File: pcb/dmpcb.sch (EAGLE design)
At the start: 63 parts, among them IC1 7805DT, IC2 L293D, IC3 MAX7219CNG, IC4 LM358D, IC5 LM358D, J7 SJ-3523-SMT-TR, Q1 IRF530, Q2 IRF530

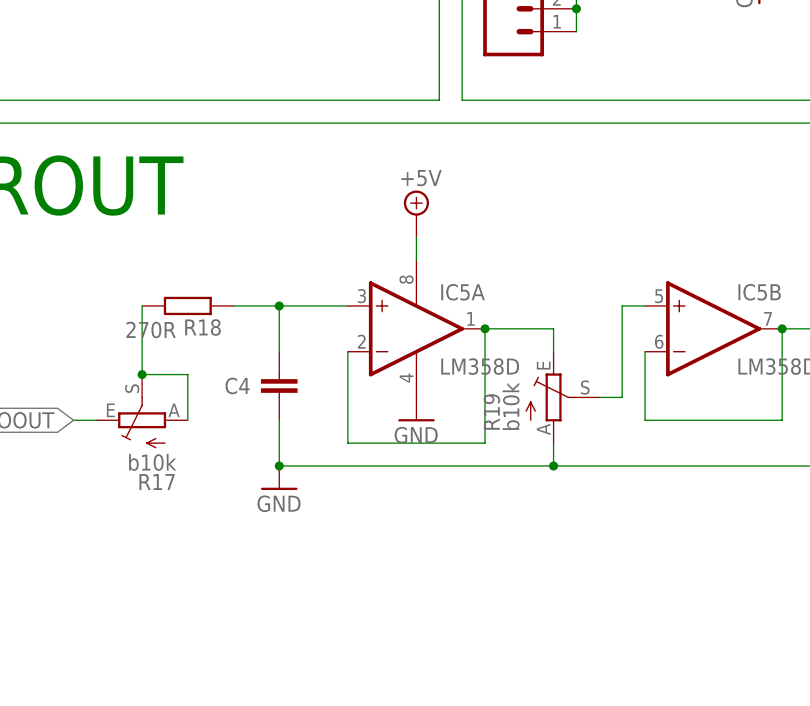
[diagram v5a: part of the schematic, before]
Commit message: added missing decoupling cap
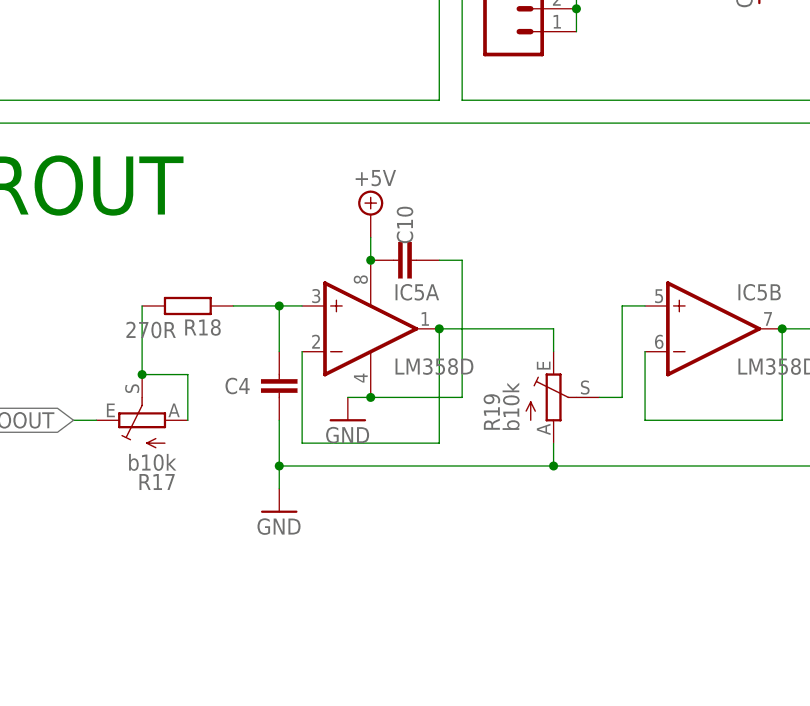
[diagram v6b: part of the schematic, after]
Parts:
- added C10: 100nf, rcl:C-EUC0805
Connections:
- net +5V: now also C10.2
- net GND: now also C10.1
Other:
- moved on the sheet: IC5A
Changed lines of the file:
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@@
 <part name="GND26" library="supply1" library_urn="urn:adsk.eagle:library:371" deviceset="GND" device=""/>
 <part name="GND28" library="supply1" library_urn="urn:adsk.eagle:library:371" deviceset="GND" device=""/>
+<part name="C10" library="rcl" library_urn="urn:adsk.eagle:library:334" deviceset="C-EU" device="C0805" package3d_urn="urn:adsk.eagle:package:23617/2" value="100nf"/>
 </parts>
 <sheets>
@@
 <attribute name="NAME" x="291.084" y="-35.179" size="1.778" layer="95"/>
 </instance>
-<instance part="IC5" gate="A" x="312.42" y="-27.94" smashed="yes">
-<attribute name="NAME" x="314.96" y="-24.765" size="1.778" layer="95"/>
-<attribute name="VALUE" x="314.96" y="-33.02" size="1.778" layer="96"/>
+<instance part="IC5" gate="A" x="307.34" y="-27.94" smashed="yes">
+<attribute name="NAME" x="309.88" y="-24.765" size="1.778" layer="95"/>
+<attribute name="VALUE" x="309.88" y="-33.02" size="1.778" layer="96"/>
 </instance>
 <instance part="R19" gate="1" x="327.66" y="-35.56" smashed="yes">
@@
 <attribute name="VALUE" x="195.58" y="-45.72" size="1.778" layer="96"/>
 </instance>
-<instance part="IC5" gate="P" x="312.42" y="-27.94" smashed="yes"/>
-<instance part="SUPPLY14" gate="+5V" x="312.42" y="-15.24" smashed="yes">
-<attribute name="VALUE" x="310.515" y="-12.065" size="1.778" layer="96"/>
-</instance>
-<instance part="GND26" gate="1" x="312.42" y="-38.1" smashed="yes">
-<attribute name="VALUE" x="309.88" y="-40.64" size="1.778" layer="96"/>
-</instance>
-<instance part="GND28" gate="1" x="297.18" y="-45.72" smashed="yes">
-<attribute name="VALUE" x="294.64" y="-48.26" size="1.778" layer="96"/>
+<instance part="IC5" gate="P" x="307.34" y="-27.94" smashed="yes"/>
+<instance part="SUPPLY14" gate="+5V" x="307.34" y="-15.24" smashed="yes">
+<attribute name="VALUE" x="305.435" y="-12.065" size="1.778" layer="96"/>
+</instance>
+<instance part="GND26" gate="1" x="304.8" y="-38.1" smashed="yes">
+<attribute name="VALUE" x="302.26" y="-40.64" size="1.778" layer="96"/>
+</instance>
+<instance part="GND28" gate="1" x="297.18" y="-48.26" smashed="yes">
+<attribute name="VALUE" x="294.64" y="-50.8" size="1.778" layer="96"/>
+</instance>
+<instance part="C10" gate="G$1" x="312.42" y="-20.32" smashed="yes" rot="R270">
+<attribute name="NAME" x="310.261" y="-14.224" size="1.778" layer="95" rot="R270"/>
 </instance>
 </instances>
@@
 <pinref part="IC5" gate="P" pin="V-"/>
 <pinref part="GND26" gate="1" pin="GND"/>
-</segment>
-<segment>
+<wire x1="307.34" y1="-35.56" x2="304.8" y2="-35.56" width="0.1524" layer="91"/>
+<wire x1="307.34" y1="-35.56" x2="317.5" y2="-35.56" width="0.1524" layer="91"/>
+<junction x="307.34" y="-35.56"/>
+<wire x1="317.5" y1="-35.56" x2="317.5" y2="-20.32" width="0.1524" layer="91"/>
+<wire x1="317.5" y1="-20.32" x2="314.96" y2="-20.32" width="0.1524" layer="91"/>
+<pinref part="C10" gate="G$1" pin="1"/>
+</segment>
+<segment>
+<pinref part="GND28" gate="1" pin="GND"/>
 <pinref part="C4" gate="G$1" pin="2"/>
 <wire x1="297.18" y1="-38.1" x2="297.18" y2="-43.18" width="0.1524" layer="91"/>
-<wire x1="297.18" y1="-43.18" x2="327.66" y2="-43.18" width="0.1524" layer="91"/>
 <pinref part="R19" gate="1" pin="A"/>
+<wire x1="297.18" y1="-43.18" x2="297.18" y2="-45.72" width="0.1524" layer="91"/>
 <wire x1="327.66" y1="-43.18" x2="327.66" y2="-40.64" width="0.1524" layer="91"/>
 <wire x1="327.66" y1="-43.18" x2="370.84" y2="-43.18" width="0.1524" layer="91"/>
-<junction x="327.66" y="-43.18"/>
 <pinref part="J7" gate="G$1" pin="1"/>
 <wire x1="370.84" y1="-43.18" x2="370.84" y2="-33.02" width="0.1524" layer="91"/>
 <wire x1="370.84" y1="-33.02" x2="375.92" y2="-33.02" width="0.1524" layer="91"/>
-<pinref part="GND28" gate="1" pin="GND"/>
+<wire x1="327.66" y1="-43.18" x2="297.18" y2="-43.18" width="0.1524" layer="91"/>
+<junction x="327.66" y="-43.18"/>
 <junction x="297.18" y="-43.18"/>
 </segment>
@@
 <pinref part="SUPPLY14" gate="+5V" pin="+5V"/>
 <pinref part="IC5" gate="P" pin="V+"/>
-<wire x1="312.42" y1="-17.78" x2="312.42" y2="-20.32" width="0.1524" layer="91"/>
+<wire x1="307.34" y1="-17.78" x2="307.34" y2="-20.32" width="0.1524" layer="91"/>
+<pinref part="C10" gate="G$1" pin="2"/>
+<junction x="307.34" y="-20.32"/>
 </segment>
 </net>
@@
 <wire x1="292.1" y1="-25.4" x2="297.18" y2="-25.4" width="0.1524" layer="91"/>
 <wire x1="297.18" y1="-25.4" x2="297.18" y2="-30.48" width="0.1524" layer="91"/>
-<wire x1="297.18" y1="-25.4" x2="304.8" y2="-25.4" width="0.1524" layer="91"/>
+<wire x1="297.18" y1="-25.4" x2="299.72" y2="-25.4" width="0.1524" layer="91"/>
 <junction x="297.18" y="-25.4"/>
 <pinref part="IC5" gate="A" pin="+IN"/>
@@
 <net name="N$69" class="0">
 <segment>
-<wire x1="304.8" y1="-30.48" x2="304.8" y2="-40.64" width="0.1524" layer="91"/>
-<wire x1="304.8" y1="-40.64" x2="320.04" y2="-40.64" width="0.1524" layer="91"/>
-<wire x1="320.04" y1="-40.64" x2="320.04" y2="-27.94" width="0.1524" layer="91"/>
-<wire x1="320.04" y1="-27.94" x2="327.66" y2="-27.94" width="0.1524" layer="91"/>
+<wire x1="299.72" y1="-30.48" x2="299.72" y2="-40.64" width="0.1524" layer="91"/>
+<wire x1="299.72" y1="-40.64" x2="314.96" y2="-40.64" width="0.1524" layer="91"/>
+<wire x1="314.96" y1="-40.64" x2="314.96" y2="-27.94" width="0.1524" layer="91"/>
+<wire x1="314.96" y1="-27.94" x2="327.66" y2="-27.94" width="0.1524" layer="91"/>
 <wire x1="327.66" y1="-27.94" x2="327.66" y2="-30.48" width="0.1524" layer="91"/>
 <pinref part="R19" gate="1" pin="E"/>
 <pinref part="IC5" gate="A" pin="-IN"/>
 <pinref part="IC5" gate="A" pin="OUT"/>
-<junction x="320.04" y="-27.94"/>
-</segment>
-</net>
+<junction x="314.96" y="-27.94"/>
+</segment>
+</net>

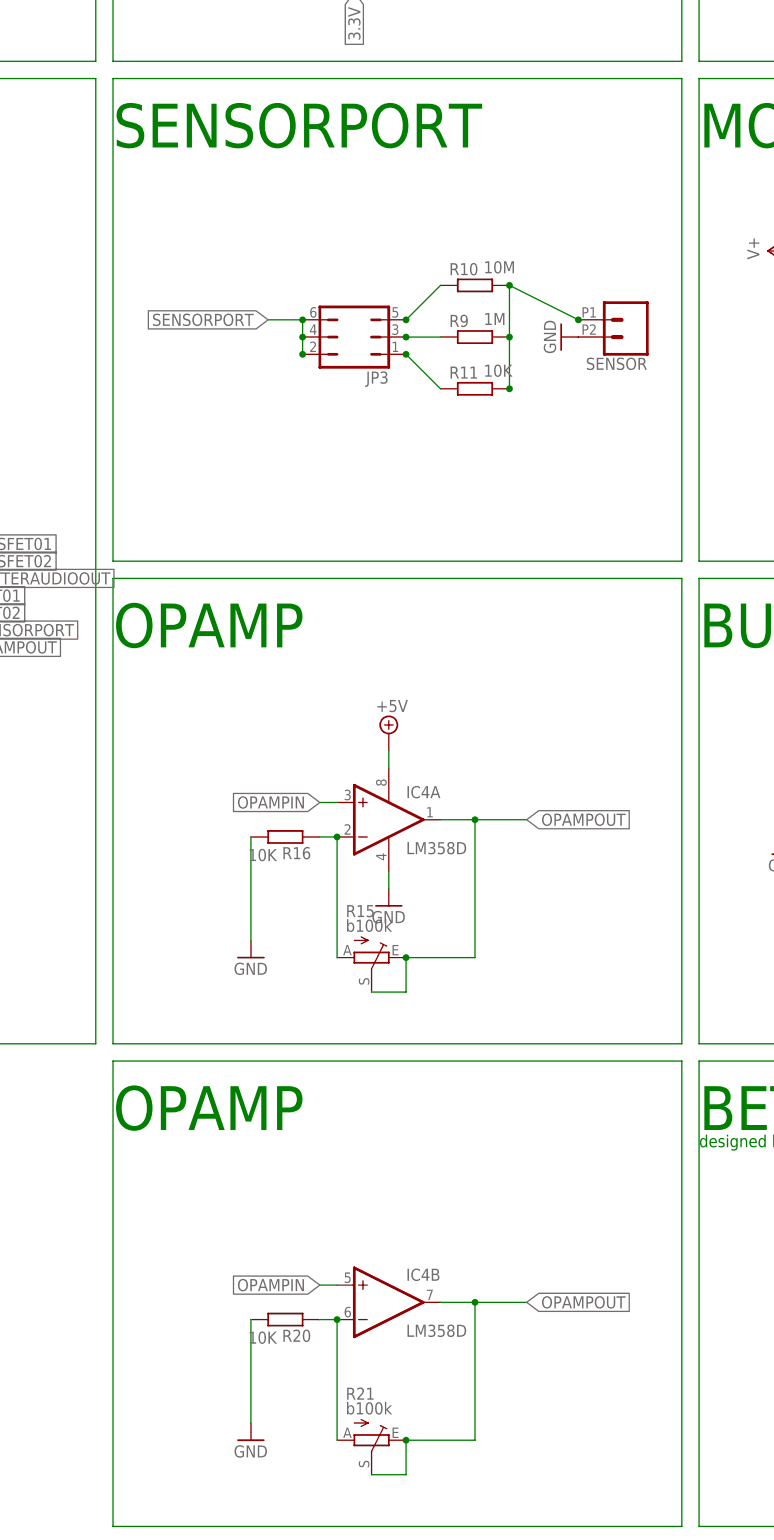
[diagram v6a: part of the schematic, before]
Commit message: corrected sensorport and changed the second half of the lm358 to a freely user-configurable setup
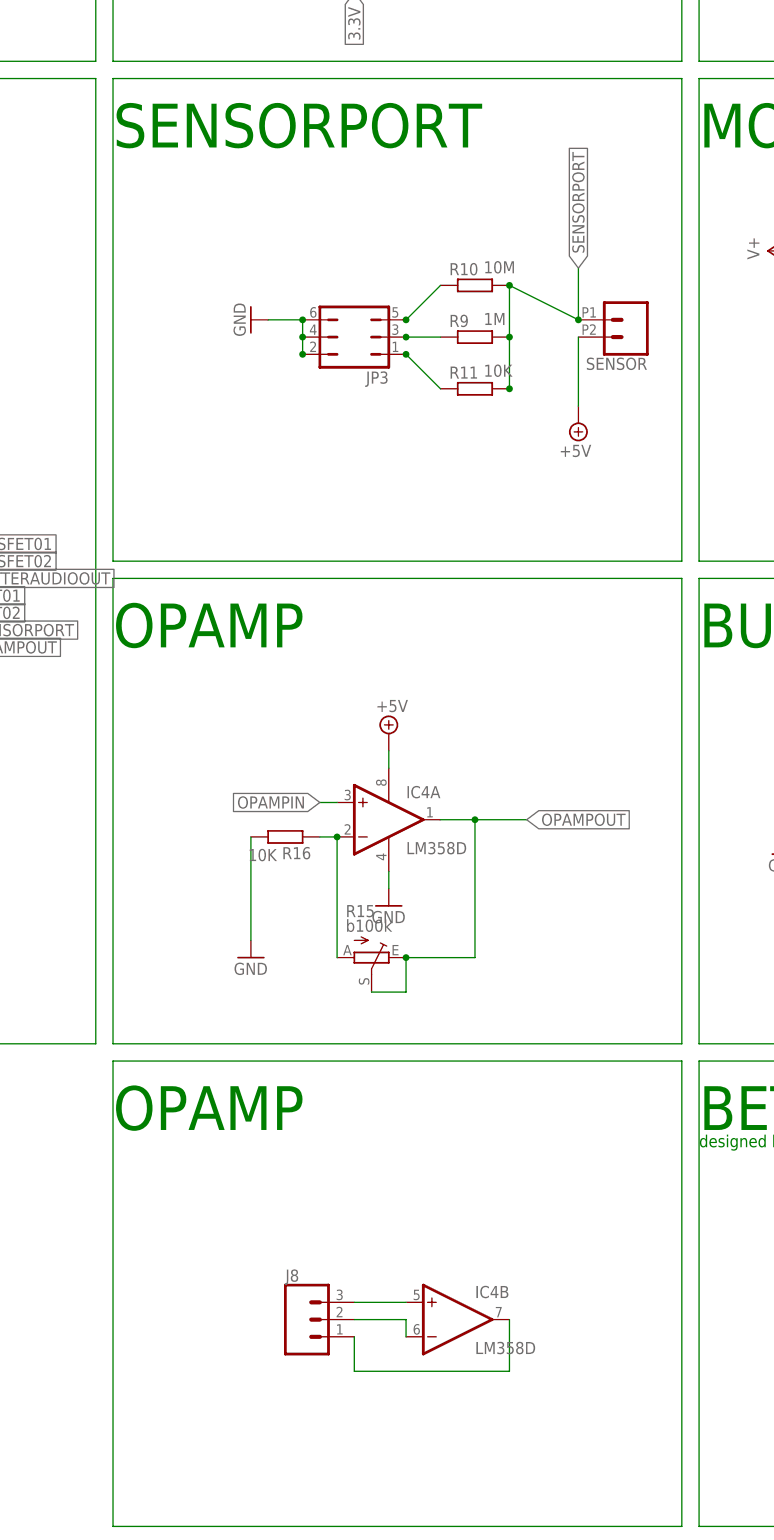
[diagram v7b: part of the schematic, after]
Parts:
- removed R20: 10K, rcl:R-EU_M0805
- removed R21: b100k, pot:TRIM_EU-RJ9W
- added J8: (no value), SparkFun-Connectors:CONN_03LOCK_LONGPADS
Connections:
- new net N$70: IC4B.-IN, J8.2
- net +5V: now also SENSOR.2
- net GND: now also JP3.2, JP3.4, JP3.6; no longer R20.2, SENSOR.2
- net N$20: now also IC4B.+IN, J8.3; no longer R10.2, R11.2, R9.2, SENSOR.1
- net N$75: now also IC4B.OUT, J8.1; no longer IC4B.-IN, R20.1, R21.A
- net OPAMPIN: no longer IC4B.+IN
- net OPAMPOUT: no longer IC4B.OUT, R21.E, R21.S
- net SENSORPORT: now also R10.2, R11.2, R9.2, SENSOR.1; no longer JP3.2, JP3.4, JP3.6
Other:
- moved on the sheet: IC4B
